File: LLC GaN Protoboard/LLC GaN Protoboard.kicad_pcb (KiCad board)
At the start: 2 copper layers, 51.3 x 150 mm, 27 parts, among them IC1 FAN73912AMX, IC2 BZX84-C5V6,215, IC3 BZX84-C5V6,215, IC4 GAN7R0-150LBE, IC5 GAN7R0-150LBE, IC6 BZX84-C5V6,215, J1 Conn_02x10_Top_Bottom, J2 Conn_02x10_Top_Bottom

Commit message: Edited layout
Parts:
- added C4: .1u, Capacitor_SMD:C_0603_1608Metric, F.Cu at (60.5, 72.5)
- added C5: 2.2u, Capacitor_SMD:C_0603_1608Metric, F.Cu at (61.0, 68.5)
- added C6: 1u, Capacitor_SMD:C_0603_1608Metric, F.Cu at (73.0, 93.0)
- added C7: 1u, Capacitor_SMD:C_0603_1608Metric, F.Cu at (73.2, 97.6)
- added C8: 22u, Capacitor_SMD:C_0603_1608Metric, F.Cu at (74.0, 78.0)
- added L1: SRR1260-150M, inductor:IND_BOURNS_SRR1260, F.Cu at (72.6, 62.0)
- added R4: 118k, Resistor_SMD:R_2010_5025Metric, F.Cu at (70.0, 73.5)
- added R5: 22.1k, Resistor_SMD:R_2010_5025Metric, F.Cu at (70.0, 81.5)
- added U1: PLMR54410DBVR, buck_conv:U_SOT-23_TEX, F.Cu at (60.1, 78.0)
- moved TP3 49.1 mm to (57.5, 88.0)
- moved IC6 39.2 mm to (99.7, 110.0), turned to 90 degrees
- moved TP2 38.6 mm to (67.0, 88.0)
- moved R1 36.2 mm to (95.2, 115.6), turned to -90 degrees
- moved TP4 35.0 mm to (62.5, 157.5)
- moved C1 28.8 mm to (90.2, 114.1), turned to -90 degrees
- moved TP1 26.3 mm to (82.5, 94.0), turned to 90 degrees
- moved IC3 25.0 mm to (77.4, 90.5)
- moved IC5 24.9 mm to (77.4, 86.0)
- moved CBOOT1 24.8 mm to (87.5, 86.7)
- moved R3 16.3 mm to (66.0, 95.0)
- moved C2 16.0 mm to (68.0, 148.5)
- moved C3 16.0 mm to (74.5, 171.0)
- moved D1 16.0 mm to (87.5, 162.5)
- moved D2 16.0 mm to (77.0, 162.5)
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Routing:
- net GND: vias 0 -> 1
- net /LLC/IIN_HIGH: vias 0 -> 1
- net (no net): vias 2 -> 0
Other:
- outline, holes or cut-outs redrawn

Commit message: first route
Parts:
- added C10: 1n, Capacitor_SMD:C_0603_1608Metric, F.Cu at (92.5, 116.5)
- added C9: 1n, Capacitor_SMD:C_0603_1608Metric, F.Cu at (99.5, 116.5)
- added D5: ADS12B3-ASARH, ADS12B3-ASARH:ADS12B3ASARH, F.Cu at (84.0, 79.0)
- added D6: ADS12B3-ASARH, ADS12B3-ASARH:ADS12B3ASARH, F.Cu at (98.0, 122.5)
- added D7: ADS12B3-ASARH, ADS12B3-ASARH:ADS12B3ASARH, F.Cu at (91.0, 122.5)
- added IC7: AMC1200SDUBR, AMC1200SDUBR:SOP254P1040X485-8N, F.Cu at (51.0, 170.7)
- added IC8: AMC1200SDUBR, AMC1200SDUBR:SOP254P1040X485-8N, F.Cu at (51.0, 158.5)
- added PS1: CME0303S3C, CME0303S3C:CME0303S3C, F.Cu at (46.7, 148.4)
- added R10: 10k, Resistor_SMD:R_0603_1608Metric_Pad0.98x0.95mm_HandSolder, F.Cu at (41.0, 121.5)
- added R11: 10k, Resistor_SMD:R_0603_1608Metric_Pad0.98x0.95mm_HandSolder, F.Cu at (43.0, 121.5)
- added R12: 10k, Resistor_SMD:R_0603_1608Metric_Pad0.98x0.95mm_HandSolder, F.Cu at (42.0, 118.5)
- added R13: 10k, Resistor_SMD:R_0603_1608Metric_Pad0.98x0.95mm_HandSolder, F.Cu at (42.5, 126.0)
- added R14: 10k, Resistor_SMD:R_0603_1608Metric_Pad0.98x0.95mm_HandSolder, F.Cu at (58.0, 125.5)
- added R15: 10k, Resistor_SMD:R_0603_1608Metric_Pad0.98x0.95mm_HandSolder, F.Cu at (54.0, 130.0)
- added R16: 10k, Resistor_SMD:R_0603_1608Metric_Pad0.98x0.95mm_HandSolder, F.Cu at (45.5, 129.5)
- added R17: 20k, Resistor_SMD:R_0603_1608Metric_Pad0.98x0.95mm_HandSolder, F.Cu at (51.5, 130.0)
- added R18: 20k, Resistor_SMD:R_0603_1608Metric_Pad0.98x0.95mm_HandSolder, F.Cu at (55.5, 125.5)
- added R19: 90k, Resistor_THT:R_Axial_Power_L38.0mm_W6.4mm_P45.72mm, F.Cu at (45.6, 197.5)
- added R20: 1k, Resistor_SMD:R_1210_3225Metric_Pad1.30x2.65mm_HandSolder, F.Cu at (45.5, 190.0)
- added R21: 1, Resistor_SMD:R_0603_1608Metric_Pad0.98x0.95mm_HandSolder, F.Cu at (85.7, 123.7)
- added R22: 1, Resistor_SMD:R_0603_1608Metric_Pad0.98x0.95mm_HandSolder, F.Cu at (74.2, 123.7)
- added R6: R, Resistor_SMD:R_0603_1608Metric_Pad0.98x0.95mm_HandSolder, F.Cu at (96.9, 143.5)
- added R7: 1k, Resistor_SMD:R_0603_1608Metric_Pad0.98x0.95mm_HandSolder, F.Cu at (96.0, 115.5)
- added R8: 1k, Resistor_SMD:R_0603_1608Metric_Pad0.98x0.95mm_HandSolder, F.Cu at (89.0, 115.5)
- added R9: 10k, Resistor_SMD:R_0603_1608Metric_Pad0.98x0.95mm_HandSolder, F.Cu at (42.0, 116.5)
- added TP10: 5019, 5019:5019, F.Cu at (116.5, 91.5)
- added TP11: 5019, 5019:5019, F.Cu at (116.5, 96.6)
- added TP14: 5019, 5019:5019, F.Cu at (70.0, 112.2)
- added TP15: 5019, 5019:5019, F.Cu at (115.5, 134.6)
- added TP16: 5019, 5019:5019, F.Cu at (107.5, 114.0)
- added TP17: 5019, 5019:5019, F.Cu at (67.7, 127.7)
- added TP19: 5019, 5019:5019, F.Cu at (121.0, 120.5)
- added TP20: 5019, 5019:5019, F.Cu at (54.8, 139.4)
- added TP21: 5019, 5019:5019, F.Cu at (46.8, 139.4)
- added TP22: 5019, 5019:5019, F.Cu at (55.5, 186.0)
- added TP23: 5019, 5019:5019, F.Cu at (43.0, 79.0)
- added TP24: 5019, 5019:5019, F.Cu at (106.5, 99.5)
- added TP25: 5019, 5019:5019, F.Cu at (28.0, 114.0)
- added TP26: 5019, 5019:5019, F.Cu at (25.0, 155.5)
- added TP9: 5019, 5019:5019, F.Cu at (116.5, 86.3)
- added U2: LM124DR, LM124DR:SOIC127P600X175-14N, F.Cu at (49.0, 123.0)
- L1: footprint inductor:IND_BOURNS_SRR1260 -> SRR1260-150M:SRR1260-150M
- R1, R4, R5: footprint Resistor_SMD:R_2010_5025Metric -> Resistor_SMD:R_0603_1608Metric_Pad0.98x0.95mm_HandSolder
- moved TP3 57.2 mm to (70.7, 143.7), turned to 0 degrees
- moved R2 55.2 mm to (101.5, 206.0), turned to 180 degrees
- moved TP2 49.3 mm to (70.7, 137.2)
- moved IC3 45.9 mm to (85.6, 135.7)
- moved R3 45.1 mm to (95.0, 129.5), turned to 0 degrees
- moved IC5 43.4 mm to (84.1, 128.8), turned to -90 degrees
- moved TP1 43.3 mm to (79.7, 137.2), turned to 0 degrees
- moved C6 41.3 mm to (84.2, 132.7), turned to 0 degrees
- moved TP8 39.3 mm to (87.0, 206.0)
- moved CBOOT1 39.0 mm to (78.7, 124.7), turned to 180 degrees
- moved C7 35.2 mm to (75.7, 132.7), turned to 0 degrees
- moved D3 32.5 mm to (69.0, 178.0), turned to 180 degrees
- moved IC4 31.9 mm to (75.6, 128.8), turned to -90 degrees
- moved IC2 30.7 mm to (71.2, 132.7)
- moved TP7 30.1 mm to (74.0, 206.0)
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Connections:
- net Net-(U1-EN) renamed /LLC/VIN_RECT
- IC4 pad 1: /LLC/GLOW -> Net-(IC4-G)
- IC5 pad 1: /LLC/GHIGH -> Net-(IC5-G)
- J1 pad 1: /Mount/+3.3V -> +3.3V
- J1 pad 11: /Mount/+5V -> +5V
- J1 pad 16: /Mount/ADCINA4/VIN -> /Sense/2OUT
- J1 pad 18: /Mount/ADCINB5/IOUT -> /Sense/3OUT
- J1 pad 6: /Mount/ADCINA9/IIN -> /Sense/1OUT
- J2 pad 1: /Mount/PWM7A/HI -> /LLC/HIN
- J2 pad 2: /Mount/PWM7B/LO -> /LLC/LIN
- R3 pad 2: /LLC/IIN_HIGH -> /LLC/VIN
- TP1 pad 1: /LLC/IIN_LOW -> /LLC/VS
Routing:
- net /LLC/VIN: track 0.00 -> 22.1 mm, vias 0 -> 1
- net /LLC/IIN_LOW: track 0.00 -> 14.6 mm
- net PGND: track 0.00 -> 3.91 mm
- net /LLC/IIN_HIGH: vias 1 -> 0
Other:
- board size 51.3 x 150 mm -> 78.4 x 170 mm

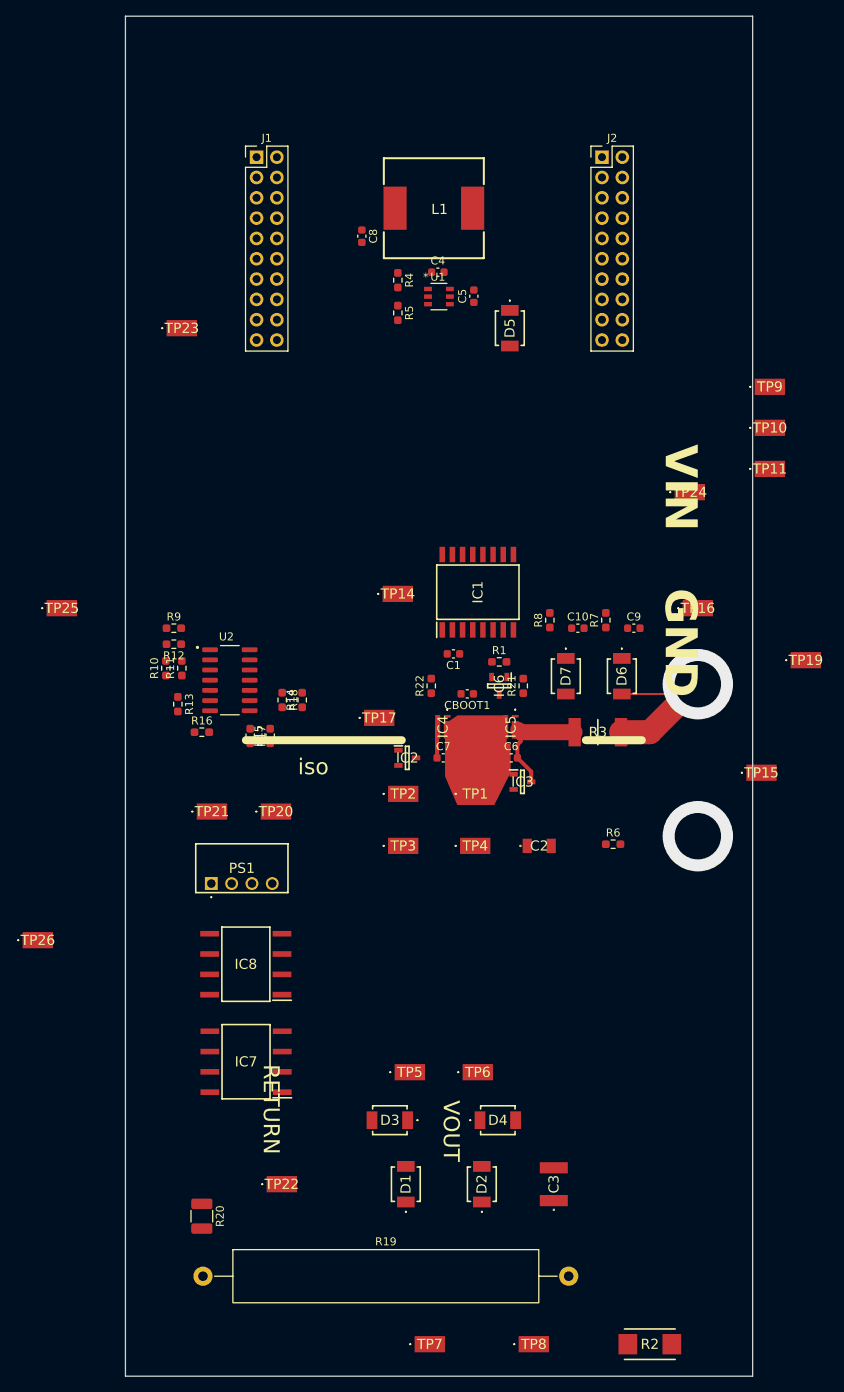
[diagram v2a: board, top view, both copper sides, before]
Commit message: Initial primary side layout
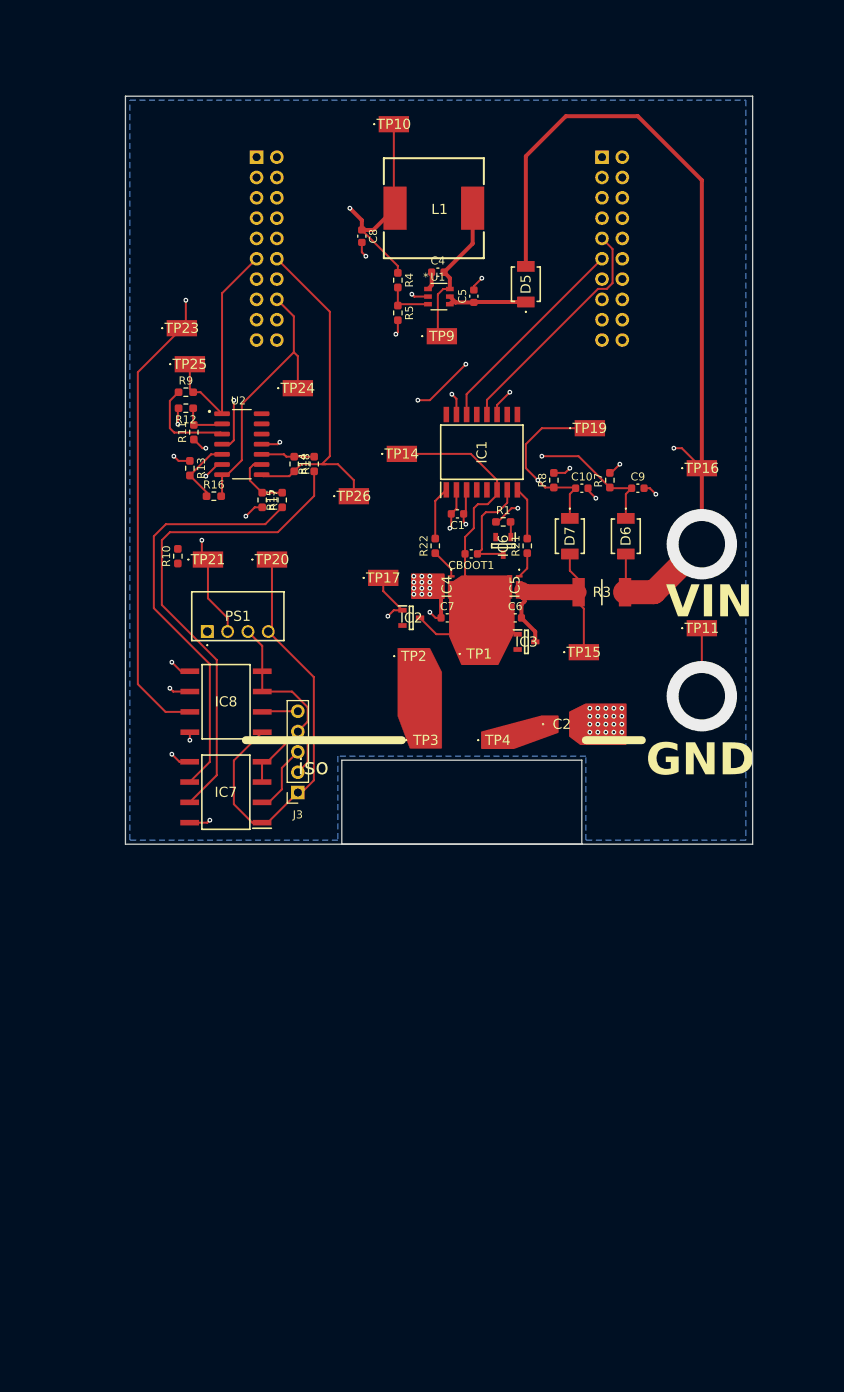
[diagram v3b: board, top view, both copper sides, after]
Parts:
- removed C3: C1812C104KDRACTU, C1812C104KDRACTU:C1812
- removed D1, D2, D3, D4: ADS12B3-ASARH, ADS12B3-ASARH:ADS12B3ASARH
- removed R19: 90k, Resistor_THT:R_Axial_Power_L38.0mm_W6.4mm_P45.72mm
- removed R2: WSC25155R000FEA, WSC25155R000FEA:RESM6438X317N
- removed R20: 1k, Resistor_SMD:R_1210_3225Metric_Pad1.30x2.65mm_HandSolder
- removed R6: R, Resistor_SMD:R_0603_1608Metric_Pad0.98x0.95mm_HandSolder
- removed TP22, TP5, TP6, TP7, TP8: 5019, 5019:5019
- added J3: Conn_01x05_Pin, Connector_PinSocket_2.54mm:PinSocket_1x05_P2.54mm_Vertical, F.Cu at (57.5, 137.0)
- J1, J2: value Conn_02x10_Top_Bottom -> Conn_02x10_Odd_Even; footprint Connector_PinHeader_2.54mm:PinHeader_2x10_P2.54mm_Vertical -> Connector_PinSocket_2.54mm:PinSocket_2x10_P2.54mm_Vertical; moved to B.Cu
- moved TP26 68.1 mm to (64.5, 100.0)
- moved TP10 60.4 mm to (69.5, 53.5)
- moved TP24 50.7 mm to (57.5, 86.5)
- moved TP9 41.5 mm to (75.5, 80.0)
- moved TP19 39.6 mm to (94.0, 91.5)
- moved TP25 34.4 mm to (44.0, 83.5)
- moved IC7 33.8 mm to (48.5, 137.0)
- moved IC8 32.9 mm to (48.5, 125.7)
- moved PS1 31.5 mm to (46.2, 116.9)
- moved TP20 31.5 mm to (54.3, 107.9)
- moved TP21 31.5 mm to (46.3, 107.9)
- moved R11 29.5 mm to (44.5, 92.0)
- moved R12 29.5 mm to (43.5, 89.0)
- moved R13 29.5 mm to (44.0, 96.5)
- moved R14 29.5 mm to (59.5, 96.0)
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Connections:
- C2 pad 2: PGND -> GND
- C7 pad 1: PGND -> GND
- IC2 pad 1: PGND -> GND
- IC4 pad 2: PGND -> GND
- IC8 pad 2: Net-(IC8-VINP) -> /Sense/VINP
- J1 pad 11: +5V -> /Sense/1OUT
- J1 pad 12: GND -> /Sense/3OUT
- J1 pad 14: unconnected-(J1-Pin_14-Pad14) -> /Mount/ADCINB4/VOUT
- J1 pad 17: /Mount/ADCINB4/VOUT -> unconnected-(J1-Pin_17-Pad17)
- J1 pad 18: /Sense/3OUT -> unconnected-(J1-Pin_18-Pad18)
- J1 pad 2: unconnected-(J1-Pin_2-Pad2) -> +5V
- J1 pad 4: unconnected-(J1-Pin_4-Pad4) -> GND
- J1 pad 6: /Sense/1OUT -> unconnected-(J1-Pin_6-Pad6)
- J2 pad 1: /LLC/HIN -> unconnected-(J2-Pin_1-Pad1)
- J2 pad 11: GND -> /Mount/PWM5B/LO
- J2 pad 16: unconnected-(J2-Pin_16-Pad16) -> /Mount/LED
- J2 pad 18: /Mount/LED -> unconnected-(J2-Pin_18-Pad18)
- J2 pad 2: /LLC/LIN -> GND
- J2 pad 9: unconnected-(J2-Pin_9-Pad9) -> /Mount/PWM5A/HI
- TP17 pad 1: PGND -> GND
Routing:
- net +3.3V: track 0.00 -> 177.3 mm, vias 0 -> 7
- net /LLC/VIN: track 22.1 -> 177.7 mm, vias 1 -> 5
- net +5V: track 0.00 -> 116.7 mm, vias 0 -> 3
- net /Mount/ADCINB4/VOUT: track 0.00 -> 70.9 mm, vias 0 -> 1
- net /Sense/INV_LOW: track 0.00 -> 68.3 mm, vias 0 -> 2
- net /Sense/INV_HIGH: track 0.00 -> 67.9 mm, vias 0 -> 2
- net /Sense/IOUT_VOUTP: track 0.00 -> 61.4 mm
- net GND: track 0.00 -> 57.6 mm, vias 1 -> 54
- net +3.3V_ISO: track 0.00 -> 53.8 mm
- net /Sense/IOUT_VOUTN: track 0.00 -> 52.2 mm
- net /Sense/3OUT: track 0.00 -> 44.4 mm
- net /LLC/VS: track 0.00 -> 38.7 mm
- net /Sense/2OUT: track 0.00 -> 34.3 mm
- net GND_ISO: track 0.00 -> 33.0 mm
- net /Mount/PWM5A/HI: track 0.00 -> 29.7 mm
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- added copper zone on B.Cu, net GND
- added copper zone on In1.Cu, net GND
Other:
- board size 78.4 x 170 mm -> 78.4 x 93.5 mm
- copper layers 2 -> 4
- rule pad_to_mask_clearance: 0.5 -> 0.1
- board text removed: "RETURN"
- board text removed: "VOUT"

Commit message: Layout for secondary
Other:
- board text added: "btanqy 2026"
- board text removed: "iso"

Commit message: Added open spots for soldering
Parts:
- added C11: 0.1u, Capacitor_SMD:C_0603_1608Metric, F.Cu at (86.2, 87.2)
- added C12: 0.1u, Capacitor_SMD:C_0603_1608Metric, F.Cu at (40.4, 138.2)
- added C13: 0.1u, Capacitor_SMD:C_0603_1608Metric, F.Cu at (56.6, 141.4)
- added C14: 0.1u, Capacitor_SMD:C_0603_1608Metric, F.Cu at (41.4, 129.8)
- added C15: 0.1u, Capacitor_SMD:C_0603_1608Metric, F.Cu at (56.6, 122.6)
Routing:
- net GND_ISO: track 33.0 -> 46.1 mm, vias 0 -> 1
- net +3.3V_ISO: track 53.8 -> 65.9 mm, vias 0 -> 2
- net +3.3V: track 177.3 -> 186.3 mm
- net GND: track 57.6 -> 62.8 mm, vias 54 -> 57

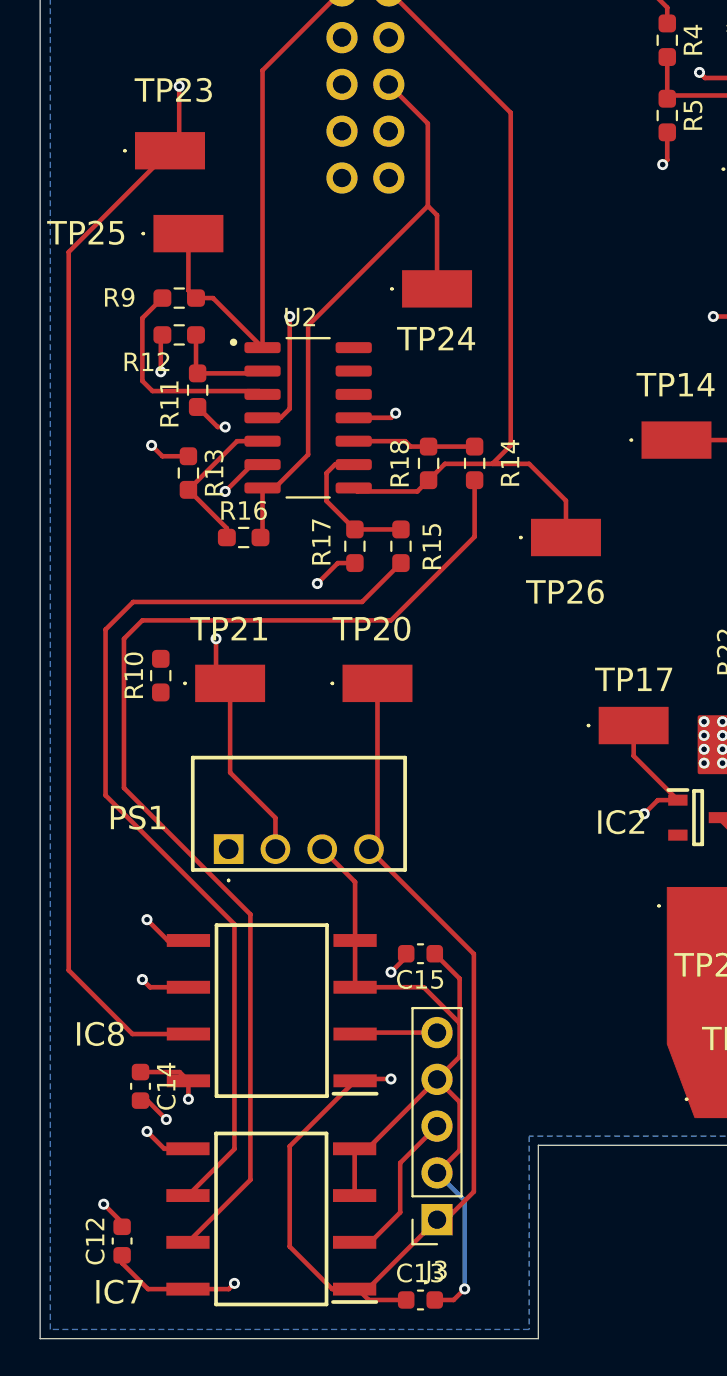
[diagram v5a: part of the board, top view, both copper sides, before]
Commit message: Added secondary clamp and swapped components
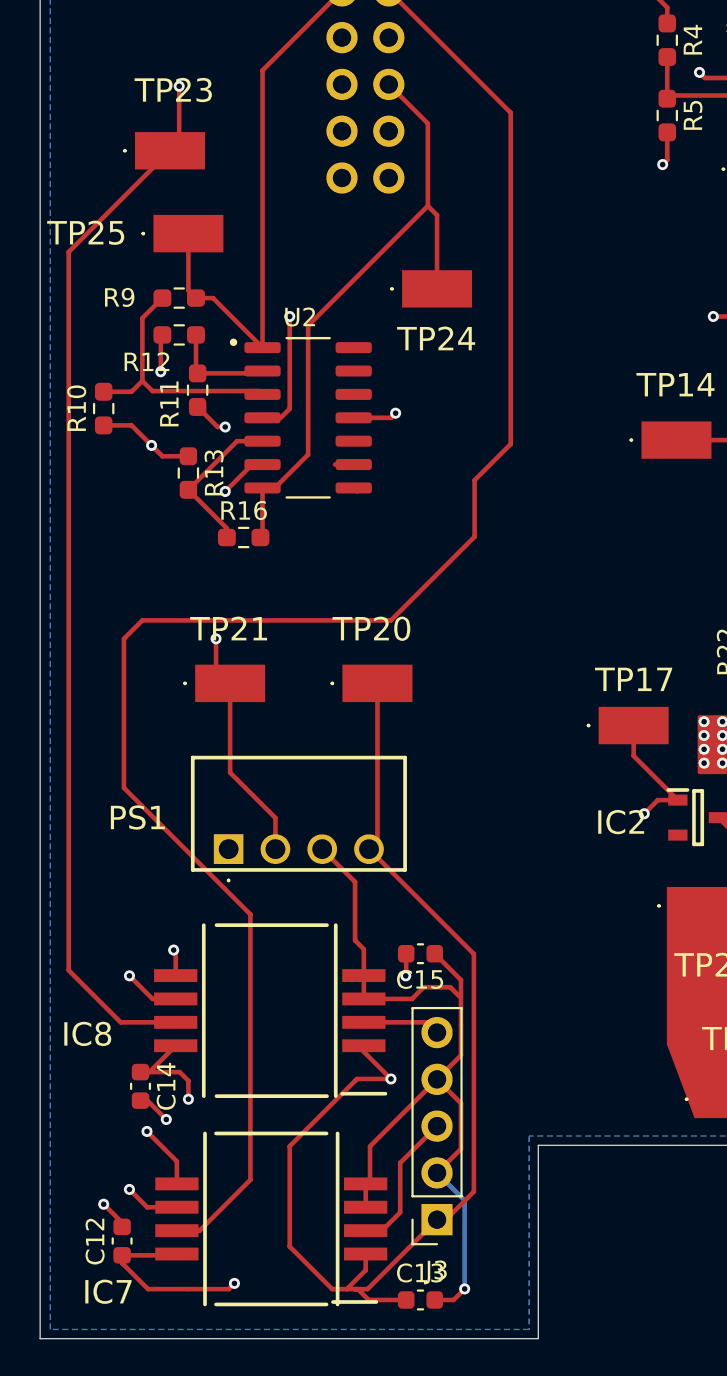
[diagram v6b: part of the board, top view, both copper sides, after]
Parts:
- removed R14, R15: 10k, Resistor_SMD:R_0603_1608Metric_Pad0.98x0.95mm_HandSolder
- removed R17, R18: 20k, Resistor_SMD:R_0603_1608Metric_Pad0.98x0.95mm_HandSolder
- removed TP26: 5019, 5019:5019
- moved R10 14.8 mm to (39.4, 93.0)
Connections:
- IC7 pad 6: /Sense/IOUT_VOUTN -> GND
- J1 pad 12: /Sense/3OUT -> /Sense/IOUT_VOUTP
- U2 pad 10: /Sense/3IN+ -> unconnected-(U2-3IN+-Pad10)
- U2 pad 8: /Sense/3OUT -> unconnected-(U2-3OUT-Pad8)
- U2 pad 9: /Sense/3IN- -> unconnected-(U2-3IN--Pad9)
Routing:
- net /Sense/IOUT_VOUTN: track 52.2 -> 0.00 mm
- net /Sense/3OUT: track 44.4 -> 0.00 mm
- net /Sense/IOUT_VOUTP: track 61.4 -> 91.9 mm
- net /Sense/3IN-: track 7.87 -> 0.00 mm
- net /Sense/3IN+: track 6.69 -> 0.00 mm
- net +3.3V_ISO: track 65.9 -> 70.7 mm
- net +3.3V: track 186.3 -> 182.3 mm, vias 7 -> 6
- net /Sense/INV_HIGH: track 67.9 -> 70.9 mm
- net GND: track 62.8 -> 65.7 mm, vias 57 -> 58
- net /Sense/1IN+: track 11.8 -> 14.1 mm
- net unconnected-(U2-3IN--Pad9): track 0.00 -> 1.02 mm
- net /Mount/ADCINB4/VOUT: track 70.9 -> 69.9 mm
- net /LLC/IOUT_HIGH: track 8.66 -> 7.80 mm
